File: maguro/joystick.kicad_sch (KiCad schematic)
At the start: 1 part

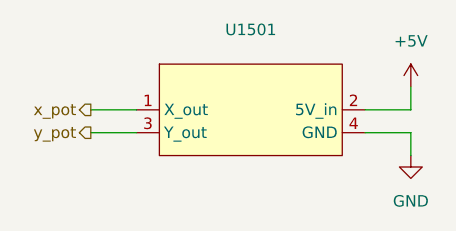
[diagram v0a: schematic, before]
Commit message: Added silkscreen
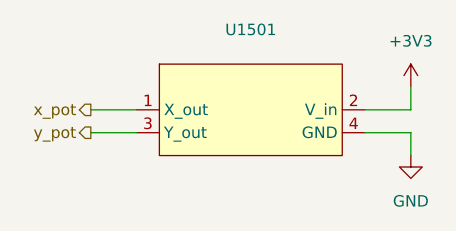
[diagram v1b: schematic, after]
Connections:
- net +5V renamed +3V3
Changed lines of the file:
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@@
-	)
-	(symbol
-		(lib_id "power:+5V")
-		(at 104.14 60.96 0)
-		(unit 1)
-		(exclude_from_sim no)
-		(in_bom yes)
-		(on_board yes)
-		(dnp no)
-		(fields_autoplaced yes)
-		(property "Reference" "#PWR01501"
-			(at 104.14 64.77 0)
-			(effects
-				(font
-					(size 1.27 1.27)
-				)
-				(hide yes)
-			)
-		)
-		(property "Value" "+5V"
-			(at 104.14 55.88 0)
-			(effects
-				(font
-					(size 1.27 1.27)
-				)
-			)
-		)
-		(property "Footprint" ""
-			(at 104.14 60.96 0)
-			(effects
-				(font
-					(size 1.27 1.27)
-				)
-				(hide yes)
-			)
-		)
-		(property "Datasheet" ""
-			(at 104.14 60.96 0)
-			(effects
-				(font
-					(size 1.27 1.27)
-				)
-				(hide yes)
-			)
-		)
-		(property "Description" "Power symbol creates a global label with name \"+5V\""
-			(at 104.14 60.96 0)
-			(effects
-				(font
-					(size 1.27 1.27)
-				)
-				(hide yes)
-			)
-		)
-		(pin "1"
-		)
-		(instances
-			(project ""
-				(path "/64a35719-70ce-4bea-be36-7f0da599755f/a6c36aed-acc7-4aeb-be6a-8df5130198de"
-					(reference "#PWR01601")
-					(unit 1)
-				)
-				(path "/64a35719-70ce-4bea-be36-7f0da599755f/f99ea653-1615-4a19-a902-af0e6be93008"
-					(reference "#PWR01501")
-					(unit 1)
-				)
-			)
-		)
 	)
 	(symbol
@@
 					(unit 1)
 				)
+			)
+		)
+	)
+	(symbol
+		(lib_id "power:+3V3")
+		(at 104.14 60.96 0)
+		(unit 1)
+		(exclude_from_sim no)
+		(in_bom yes)
+		(on_board yes)
+		(dnp no)
+		(fields_autoplaced yes)
+		(property "Reference" "#PWR01501"
+			(at 104.14 64.77 0)
+			(effects
+				(font
+					(size 1.27 1.27)
+				)
+				(hide yes)
+			)
+		)
+		(property "Value" "+3V3"
+			(at 104.14 55.88 0)
+			(effects
+				(font
+					(size 1.27 1.27)
+				)
+			)
+		)
+		(property "Footprint" ""
+			(at 104.14 60.96 0)
+			(effects
+				(font
+					(size 1.27 1.27)
+				)
+				(hide yes)
+			)
+		)
+		(property "Datasheet" ""
+			(at 104.14 60.96 0)
+			(effects
+				(font
+					(size 1.27 1.27)
+				)
+				(hide yes)
+			)
+		)
+		(property "Description" "Power symbol creates a global label with name \"+3V3\""
+			(at 104.14 60.96 0)
+			(effects
+				(font
+					(size 1.27 1.27)
+				)
+				(hide yes)
+			)
+		)
+		(pin "1"
+		)
+		(instances
+			(project ""
+				(path "/64a35719-70ce-4bea-be36-7f0da599755f/a6c36aed-acc7-4aeb-be6a-8df5130198de"
+					(reference "#PWR01601")
+					(unit 1)
+				)
+				(path "/64a35719-70ce-4bea-be36-7f0da599755f/f99ea653-1615-4a19-a902-af0e6be93008"
+					(reference "#PWR01501")
+					(unit 1)
+				)
